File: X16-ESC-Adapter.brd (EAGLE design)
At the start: 101.6 x 41.1 mm, 11 parts, among them J1 BM08B-SRSS-TB(LF)(SN)

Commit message: Now actually finished for sure
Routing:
- net GND: track 31.4 -> 32.0 mm
- added copper zone on layer 16, net GND1
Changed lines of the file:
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@@
 <via x="75.946" y="39.4208" extent="1-16" drill="0.35"/>
 <via x="75.946" y="35.3568" extent="1-16" drill="0.35"/>
-<via x="94.742" y="39.6748" extent="1-16" drill="0.35"/>
-<via x="93.4466" y="35.2552" extent="1-16" drill="0.35"/>
+<via x="93.4466" y="39.6494" extent="1-16" drill="0.35"/>
+<via x="93.472" y="35.3568" extent="1-16" drill="0.35"/>
+<polygon width="0.1524" layer="1" pour="cutout">
+<vertex x="97.79" y="34.0106"/>
+<vertex x="101.5746" y="34.0106"/>
+<vertex x="101.5746" y="-0.0254"/>
+<vertex x="97.79" y="-0.0254"/>
+</polygon>
 </signal>
 <signal name="GND">
@@
 <wire x1="61.6372" y1="38.862" x2="61.688" y2="38.9128" width="0.762" layer="1"/>
 <wire x1="61.6372" y1="38.862" x2="51.054" y2="38.862" width="0.762" layer="1"/>
-<via x="6.7564" y="39.5732" extent="1-16" drill="0.35"/>
-<via x="6.731" y="34.6202" extent="1-16" drill="0.35"/>
+<via x="7.1882" y="39.5986" extent="1-16" drill="0.35"/>
+<via x="7.2136" y="34.9504" extent="1-16" drill="0.35"/>
 <via x="36.7538" y="39.5986" extent="1-16" drill="0.35"/>
 <via x="36.7284" y="35.8394" extent="1-16" drill="0.35"/>
@@
 <contactref element="PWR" pad="NC@6"/>
 <contactref element="J1" pad="2"/>
-<wire x1="26.456" y1="36.6418" x2="26.456" y2="37.973" width="0.2032" layer="1"/>
-<wire x1="26.456" y1="37.973" x2="26.456" y2="39.4862" width="0.2032" layer="1"/>
+<wire x1="26.456" y1="36.6418" x2="26.456" y2="39.4862" width="0.2032" layer="1"/>
 <wire x1="26.456" y1="39.4862" x2="26.4668" y2="39.497" width="0.2032" layer="1"/>
 <via x="26.4668" y="39.497" extent="1-16" drill="0.35"/>
 <wire x1="19.304" y1="38.862" x2="20.5949875" y2="38.862" width="0.2032" layer="1"/>
-<wire x1="20.5949875" y1="38.862" x2="21.4441875" y2="38.0128" width="0.2032" layer="1"/>
-<wire x1="26.4162" y1="38.0128" x2="26.456" y2="37.973" width="0.2032" layer="1"/>
-<wire x1="21.4441875" y1="38.0128" x2="26.4162" y2="38.0128" width="0.2032" layer="1"/>
+<wire x1="20.5949875" y1="38.862" x2="22.9427875" y2="36.5142" width="0.2032" layer="1"/>
+<wire x1="26.456" y1="36.6418" x2="26.3284" y2="36.5142" width="0.2032" layer="1"/>
+<wire x1="26.3284" y1="36.5142" x2="22.9427875" y2="36.5142" width="0.2032" layer="1"/>
 <wire x1="26.4668" y1="39.497" x2="36.6522" y2="39.497" width="0.2032" layer="16"/>
 <wire x1="36.6522" y1="39.497" x2="36.7538" y2="39.5986" width="0.2032" layer="16"/>
-<wire x1="48.514" y1="38.862" x2="51.054" y2="38.862" width="0" layer="19" extent="1-1"/>
-<wire x1="51.054" y1="36.322" x2="51.054" y2="38.862" width="0" layer="19" extent="1-1"/>
-<wire x1="48.514" y1="36.322" x2="48.514" y2="38.862" width="0" layer="19" extent="1-1"/>
-<wire x1="45.974" y1="38.862" x2="48.514" y2="38.862" width="0" layer="19" extent="1-1"/>
-<wire x1="45.974" y1="36.322" x2="48.514" y2="36.322" width="0" layer="19" extent="1-1"/>
-<wire x1="43.434" y1="38.862" x2="45.974" y2="38.862" width="0" layer="19" extent="1-1"/>
-<wire x1="40.894" y1="38.862" x2="43.434" y2="38.862" width="0" layer="19" extent="1-1"/>
-<wire x1="43.434" y1="36.322" x2="45.974" y2="36.322" width="0" layer="19" extent="1-1"/>
-<wire x1="40.894" y1="36.322" x2="40.894" y2="38.862" width="0" layer="19" extent="1-1"/>
-<wire x1="36.7284" y1="35.8394" x2="40.894" y2="36.322" width="0" layer="19" extent="1-1"/>
-<wire x1="39.37" y1="31.5468" x2="36.7284" y2="35.8394" width="0" layer="19" extent="1-1"/>
-<wire x1="42.672" y1="31.5468" x2="39.37" y2="31.5468" width="0" layer="19" extent="1-1"/>
-<wire x1="46.45" y1="31.4114" x2="42.672" y2="31.5468" width="0" layer="19" extent="1-1"/>
-<wire x1="49.784" y1="31.5468" x2="46.45" y2="31.4114" width="0" layer="19" extent="1-1"/>
-<wire x1="46.228" y1="27.4828" x2="46.45" y2="31.4114" width="0" layer="19" extent="1-1"/>
-<wire x1="49.784" y1="27.4828" x2="46.228" y2="27.4828" width="0" layer="19" extent="1-1"/>
-<wire x1="42.672" y1="27.4828" x2="46.228" y2="27.4828" width="0" layer="19" extent="1-1"/>
-<wire x1="39.37" y1="27.4828" x2="42.672" y2="27.4828" width="0" layer="19" extent="1-1"/>
-<wire x1="36.7538" y1="39.5986" x2="36.7284" y2="35.8394" width="0" layer="19" extent="1-1"/>
-<wire x1="16.764" y1="38.862" x2="19.304" y2="38.862" width="0" layer="19" extent="1-1"/>
-<wire x1="14.224" y1="38.862" x2="16.764" y2="38.862" width="0" layer="19" extent="1-1"/>
-<wire x1="11.684" y1="38.862" x2="14.224" y2="38.862" width="0" layer="19" extent="1-1"/>
-<wire x1="9.144" y1="38.862" x2="11.684" y2="38.862" width="0" layer="19" extent="1-1"/>
-<wire x1="6.7564" y1="39.5732" x2="9.144" y2="38.862" width="0" layer="19" extent="1-1"/>
-<wire x1="9.144" y1="36.322" x2="9.144" y2="38.862" width="0" layer="19" extent="1-1"/>
-<wire x1="6.731" y1="34.6202" x2="9.144" y2="36.322" width="0" layer="19" extent="1-1"/>
+<polygon width="0.1524" layer="16" pour="cutout">
+<vertex x="0.254" y="33.6296"/>
+<vertex x="3.7846" y="33.6296"/>
+<vertex x="3.8608" y="33.5534"/>
+<vertex x="3.8608" y="0.0508"/>
+<vertex x="0.0762" y="0.0508"/>
+<vertex x="0.0762" y="33.4772"/>
+<vertex x="0.1524" y="33.5534"/>
+</polygon>
+<polygon width="0.1524" layer="1" pour="cutout">
+<vertex x="0.1778" y="33.6804"/>
+<vertex x="3.9624" y="33.6804"/>
+<vertex x="3.9624" y="0.0508"/>
+<vertex x="0.1778" y="0.0508"/>
+</polygon>
+<polygon width="0.1524" layer="16" pour="cutout">
+<vertex x="6.5532" y="40.6908"/>
+<vertex x="5.7658" y="40.6908"/>
+<vertex x="5.7658" y="34.2138"/>
+<vertex x="5.6134" y="34.0614"/>
+<vertex x="6.604" y="34.0614"/>
+<vertex x="6.604" y="40.64"/>
+</polygon>
+<polygon width="0.1524" layer="1" pour="cutout">
+<vertex x="5.7658" y="40.6654"/>
+<vertex x="6.5532" y="40.6654"/>
+<vertex x="6.5532" y="34.036"/>
+<vertex x="5.6642" y="34.036"/>
+<vertex x="5.6388" y="34.0614"/>
+<vertex x="5.7658" y="34.1884"/>
+</polygon>
+<polygon width="0.1524" layer="1">
+<vertex x="96.0374" y="40.1828"/>
+<vertex x="94.488" y="40.1828"/>
+<vertex x="94.4626" y="40.1574"/>
+<vertex x="94.4626" y="34.6456"/>
+<vertex x="94.5388" y="34.5694"/>
+<vertex x="95.6818" y="34.5694"/>
+<vertex x="95.7326" y="34.6202"/>
+<vertex x="95.7326" y="39.878"/>
+</polygon>
+<polygon width="0.1524" layer="16" pour="cutout">
+<vertex x="94.3991" y="40.1828"/>
+<vertex x="96.012" y="40.1828"/>
+<vertex x="96.0374" y="40.1574"/>
+<vertex x="95.7072" y="39.8272"/>
+<vertex x="95.7072" y="34.5948"/>
+<vertex x="94.4626" y="34.5948"/>
+<vertex x="94.4626" y="40.1193"/>
+</polygon>
 </signal>
 <signal name="ESC3A">
@@
 <wire x1="63.788" y1="38.9128" x2="67.222" y2="38.9128" width="0.762" layer="1"/>
 </signal>
+<signal name="GND1">
+<polygon width="0.1524" layer="16" pour="cutout">
+<vertex x="97.79" y="33.9852"/>
+<vertex x="101.5746" y="33.9852"/>
+<vertex x="101.5746" y="-0.0254"/>
+<vertex x="97.79" y="-0.0254"/>
+</polygon>
+</signal>
 </signals>

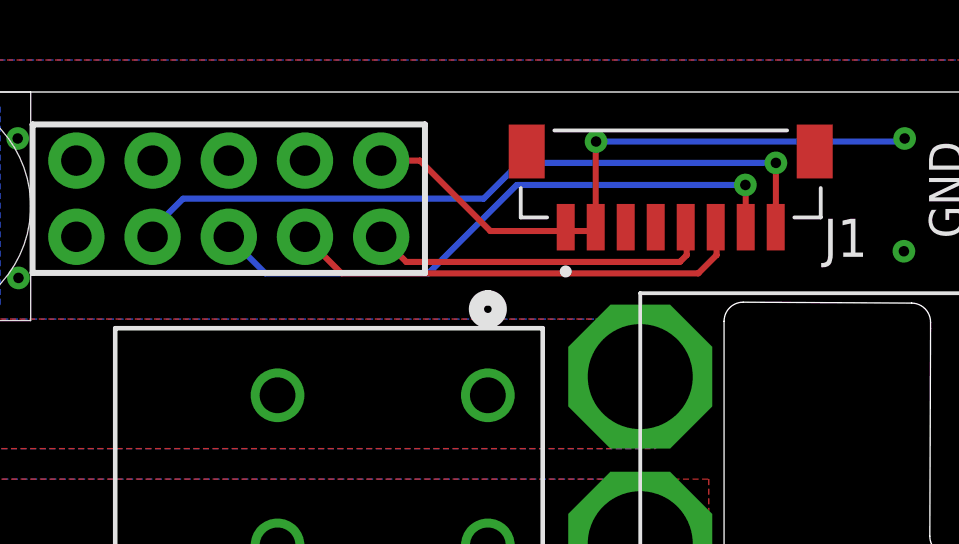
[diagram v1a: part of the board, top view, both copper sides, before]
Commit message: moved gnd trace so it doesn't overlap with pin 1 on jst
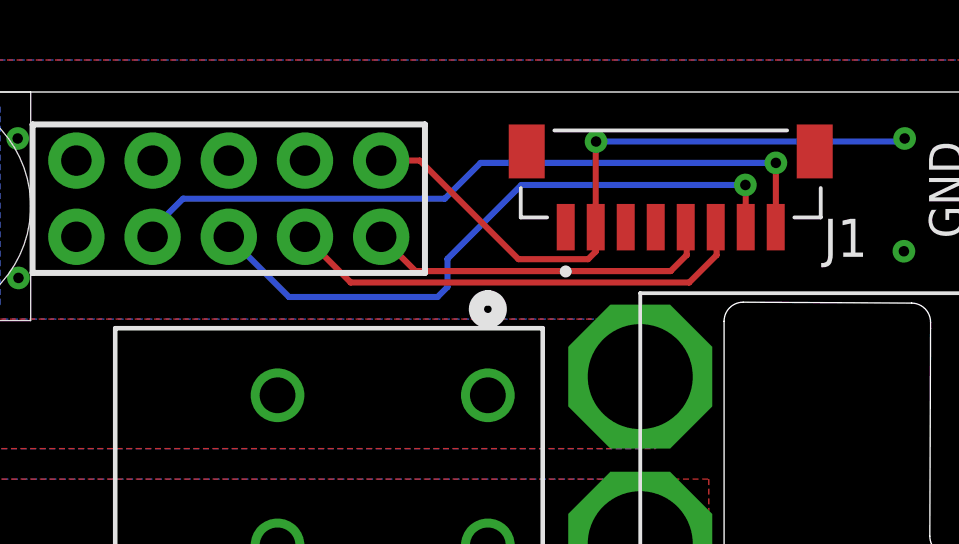
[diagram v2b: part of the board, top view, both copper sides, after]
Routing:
- net GND: track 32.0 -> 33.3 mm
- net MTR_3: track 20.4 -> 21.6 mm
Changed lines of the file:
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@@
 <wire x1="26.456" y1="39.4862" x2="26.4668" y2="39.497" width="0.2032" layer="1"/>
 <via x="26.4668" y="39.497" extent="1-16" drill="0.35"/>
-<wire x1="19.304" y1="38.862" x2="20.5949875" y2="38.862" width="0.2032" layer="1"/>
-<wire x1="20.5949875" y1="38.862" x2="22.9427875" y2="36.5142" width="0.2032" layer="1"/>
-<wire x1="26.456" y1="36.6418" x2="26.3284" y2="36.5142" width="0.2032" layer="1"/>
-<wire x1="26.3284" y1="36.5142" x2="22.9427875" y2="36.5142" width="0.2032" layer="1"/>
+<wire x1="20.5949875" y1="38.862" x2="19.304" y2="38.862" width="0.2032" layer="1"/>
+<wire x1="20.5949875" y1="38.862" x2="23.8825875" y2="35.5744" width="0.2032" layer="1"/>
+<wire x1="26.456" y1="35.829" x2="26.456" y2="36.6418" width="0.2032" layer="1"/>
+<wire x1="26.456" y1="35.829" x2="26.2014" y2="35.5744" width="0.2032" layer="1"/>
+<wire x1="26.2014" y1="35.5744" x2="23.8825875" y2="35.5744" width="0.2032" layer="1"/>
 <wire x1="26.4668" y1="39.497" x2="36.6522" y2="39.497" width="0.2032" layer="16"/>
 <wire x1="36.6522" y1="39.497" x2="36.7538" y2="39.5986" width="0.2032" layer="16"/>
@@
 <wire x1="29.456" y1="36.6418" x2="29.4894" y2="36.6084" width="0.2032" layer="1"/>
 <wire x1="29.4894" y1="36.6084" x2="29.4894" y2="35.7124" width="0.2032" layer="1"/>
-<wire x1="29.4894" y1="35.7124" x2="29.2608" y2="35.4838" width="0.2032" layer="1"/>
-<wire x1="29.2608" y1="35.4838" x2="20.1422" y2="35.4838" width="0.2032" layer="1"/>
-<wire x1="20.1422" y1="35.4838" x2="19.304" y2="36.322" width="0.2032" layer="1"/>
+<wire x1="29.4894" y1="35.7124" x2="28.956" y2="35.179" width="0.2032" layer="1"/>
+<wire x1="28.956" y1="35.179" x2="20.447" y2="35.179" width="0.2032" layer="1"/>
+<wire x1="20.447" y1="35.179" x2="19.304" y2="36.322" width="0.2032" layer="1"/>
 </signal>
 <signal name="MTR_2">
@@
 <wire x1="30.456" y1="36.6418" x2="30.4856125" y2="36.6121875" width="0.2032" layer="1"/>
 <wire x1="30.4856125" y1="36.6121875" x2="30.4856125" y2="35.7124" width="0.2032" layer="1"/>
-<wire x1="30.4856125" y1="35.7124" x2="29.8760125" y2="35.1028" width="0.2032" layer="1"/>
-<wire x1="29.8760125" y1="35.1028" x2="17.9832" y2="35.1028" width="0.2032" layer="1"/>
-<wire x1="16.764" y1="36.322" x2="17.9832" y2="35.1028" width="0.2032" layer="1"/>
+<wire x1="30.4856125" y1="35.7124" x2="29.5712125" y2="34.798" width="0.2032" layer="1"/>
+<wire x1="29.5712125" y1="34.798" x2="18.288" y2="34.798" width="0.2032" layer="1"/>
+<wire x1="16.764" y1="36.322" x2="18.288" y2="34.798" width="0.2032" layer="1"/>
 </signal>
 <signal name="MTR_3">
@@
 <wire x1="31.456" y1="38.0384" x2="31.4452" y2="38.0492" width="0.2032" layer="1"/>
 <via x="31.4452" y="38.0492" extent="1-16" drill="0.35"/>
-<wire x1="31.4452" y1="38.0492" x2="23.8252" y2="38.0492" width="0.2032" layer="16"/>
-<wire x1="23.8252" y1="38.0492" x2="20.8788" y2="35.1028" width="0.2032" layer="16"/>
-<wire x1="20.8788" y1="35.1028" x2="15.4432" y2="35.1028" width="0.2032" layer="16"/>
-<wire x1="15.4432" y1="35.1028" x2="14.224" y2="36.322" width="0.2032" layer="16"/>
+<wire x1="14.224" y1="36.322" x2="16.2306" y2="34.3154" width="0.2032" layer="16"/>
+<wire x1="21.1836" y1="34.3154" x2="21.5138" y2="34.6456" width="0.2032" layer="16"/>
+<wire x1="21.5138" y1="34.6456" x2="21.5138" y2="35.5854" width="0.2032" layer="16"/>
+<wire x1="21.5138" y1="35.5854" x2="23.9776" y2="38.0492" width="0.2032" layer="16"/>
+<wire x1="16.2306" y1="34.3154" x2="21.1836" y2="34.3154" width="0.2032" layer="16"/>
+<wire x1="23.9776" y1="38.0492" x2="31.4452" y2="38.0492" width="0.2032" layer="16"/>
 </signal>
 <signal name="MTR_4">
@@
 <contactref element="J1" pad="8"/>
 <via x="32.4612" y="38.7858" extent="1-16" drill="0.35"/>
-<wire x1="32.4612" y1="38.7858" x2="23.91329375" y2="38.7858" width="0.2032" layer="16"/>
-<wire x1="22.71949375" y1="37.592" x2="12.7" y2="37.592" width="0.2032" layer="16"/>
+<wire x1="32.4612" y1="38.7858" x2="22.61789375" y2="38.7858" width="0.2032" layer="16"/>
+<wire x1="21.42409375" y1="37.592" x2="12.7" y2="37.592" width="0.2032" layer="16"/>
 <wire x1="12.7" y1="37.592" x2="11.684" y2="36.576" width="0.2032" layer="16"/>
 <wire x1="11.684" y1="36.576" x2="11.684" y2="36.322" width="0.2032" layer="16"/>
 <wire x1="32.4612" y1="38.7858" x2="32.4612" y2="36.647" width="0.2032" layer="1"/>
 <wire x1="32.456" y1="36.6418" x2="32.4612" y2="36.647" width="0.2032" layer="1"/>
-<wire x1="23.91329375" y1="38.7858" x2="22.71949375" y2="37.592" width="0.2032" layer="16"/>
+<wire x1="22.61789375" y1="38.7858" x2="21.42409375" y2="37.592" width="0.2032" layer="16"/>
 </signal>
 <signal name="N$1">
@@
 <mfgpreviewcolor name="substratecolor" color="0xFF786E46"/>
 </mfgpreviewcolors>
+<errors>
+</errors>
 </board>
 </drawing>

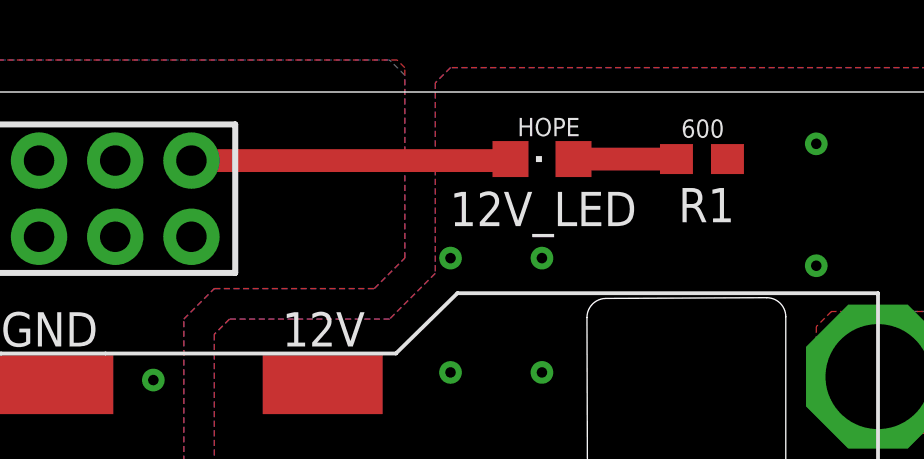
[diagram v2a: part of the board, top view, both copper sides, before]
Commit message: added junctions + moved LED to left
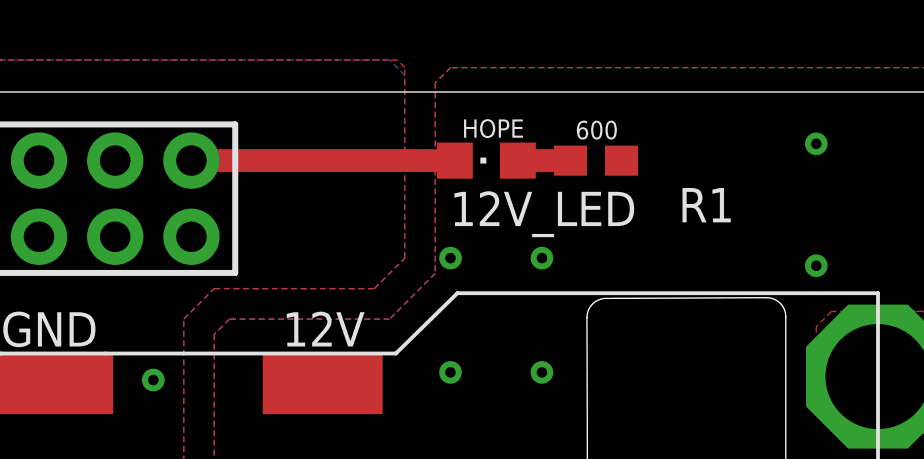
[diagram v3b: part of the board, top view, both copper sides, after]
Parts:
- moved 600 3.53 mm to (64.5, 38.9)
- moved HOPE 1.85 mm to (60.9, 38.9)
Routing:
- net GND: track 33.3 -> 31.4 mm
- net N$1: track 3.43 -> 1.76 mm
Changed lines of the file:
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@@
 <drawing>
 <settings>
-<setting alwaysvectorfont="yes"/>
+<setting alwaysvectorfont="no"/>
 <setting verticaltext="up"/>
 </settings>
@@
 <attribute name="VALUE" x="92.0242" y="35.0774" size="1.27" layer="27" ratio="6" rot="SR270"/>
 </element>
-<element name="600" library="SparkFun-Resistors" library_urn="urn:adsk.eagle:library:532" package="0603" package3d_urn="urn:adsk.eagle:package:41389018/1" value="600" x="68.072" y="38.9128" smashed="yes" rot="R180">
-<attribute name="NAME" x="68.0974" y="40.2336" size="0.6096" layer="25" font="vector" ratio="20" rot="R180" align="bottom-center"/>
-<attribute name="PROD_ID" value="RES-15715" x="68.072" y="38.9128" size="1.778" layer="27" rot="R180" display="off"/>
-<attribute name="VALUE" x="68.072" y="39.6748" size="0.6096" layer="27" font="vector" ratio="20" rot="R180" align="top-center" display="off"/>
+<element name="600" library="SparkFun-Resistors" library_urn="urn:adsk.eagle:library:532" package="0603" package3d_urn="urn:adsk.eagle:package:41389018/1" value="600" x="64.5414" y="38.862" smashed="yes" rot="R180">
+<attribute name="NAME" x="64.5668" y="40.1828" size="0.6096" layer="25" font="vector" ratio="20" rot="R180" align="bottom-center"/>
+<attribute name="PROD_ID" value="RES-15715" x="64.5414" y="38.862" size="1.778" layer="27" rot="R180" display="off"/>
+<attribute name="VALUE" x="64.5414" y="39.624" size="0.6096" layer="27" font="vector" ratio="20" rot="R180" align="top-center" display="off"/>
 </element>
-<element name="HOPE" library="led" library_urn="urn:adsk.eagle:library:259" package="CHIPLED_0805" package3d_urn="urn:adsk.eagle:package:15821/2" value="" x="62.738" y="38.9128" smashed="yes" rot="R90">
-<attribute name="NAME" x="64.008" y="40.2844" size="0.6096" layer="25" rot="R180"/>
-<attribute name="POPULARITY" value="52" x="62.738" y="38.9128" size="1.778" layer="27" rot="R90" display="off"/>
-<attribute name="VALUE" x="64.008" y="41.4528" size="1.27" layer="27" rot="R180"/>
+<element name="HOPE" library="led" library_urn="urn:adsk.eagle:library:259" package="CHIPLED_0805" package3d_urn="urn:adsk.eagle:package:15821/2" value="" x="60.8838" y="38.862" smashed="yes" rot="R90">
+<attribute name="NAME" x="62.1538" y="40.2336" size="0.6096" layer="25" rot="R180"/>
+<attribute name="POPULARITY" value="52" x="60.8838" y="38.862" size="1.778" layer="27" rot="R90" display="off"/>
+<attribute name="VALUE" x="62.1538" y="41.402" size="1.27" layer="27" rot="R180"/>
 </element>
 <element name="J1" library="X16-ESC-Adapter" package="JST_BM08B-SRSS-TB(LF)(SN)" value="BM08B-SRSS-TB(LF)(SN)" x="28.956" y="39.1668" smashed="yes">
@@
 <vertex x="57.658" y="42.2148"/>
 </polygon>
-<wire x1="61.6372" y1="38.862" x2="61.688" y2="38.9128" width="0.762" layer="1"/>
-<wire x1="61.6372" y1="38.862" x2="51.054" y2="38.862" width="0.762" layer="1"/>
+<wire x1="59.8338" y1="38.862" x2="51.054" y2="38.862" width="0.762" layer="1"/>
 <via x="7.1882" y="39.5986" extent="1-16" drill="0.35"/>
 <via x="7.2136" y="34.9504" extent="1-16" drill="0.35"/>
@@
 <contactref element="600" pad="2"/>
 <contactref element="HOPE" pad="A"/>
-<wire x1="63.788" y1="38.9128" x2="67.222" y2="38.9128" width="0.762" layer="1"/>
+<wire x1="63.6914" y1="38.862" x2="61.9338" y2="38.862" width="0.762" layer="1"/>
 </signal>
 <signal name="GND1">
